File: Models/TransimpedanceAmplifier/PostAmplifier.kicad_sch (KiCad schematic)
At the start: 16 parts, among them Q3 Q_PNP, Q4 Q_NPN, U6 OP37GSZ

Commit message: Save progress
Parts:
- removed JP1: Jumper_2_Bridged, symbol Jumper:Jumper_2_Bridged
- added J1: Conn_01x02_Pin, symbol Connector:Conn_01x02_Pin
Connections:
- net Clamped_Output: now also J1.1 (Pin_1)
- net Feedback_Terminal: now also J1.2 (Pin_2)
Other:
- note added: "Jumper connected by default"
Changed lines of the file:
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@@
 	(text "Cannot \"suppress the influence of transistor\nleakage currents or parasitic capacitances on\nthe input of OP2\" b/c the connection point is\na nonzero voltage instead of GND with this\ndesign. The approach used in the original\npaper would make the diodes conduct from the\nvoltage differential between the connection\npoint and (10k) * (±25 nA) ≈ (±0.25 mV).\n\nInstead, provide a reversible (THT) jumper\nto disconnect this feedback path if it proves\nproblematic. Omit the jumper once we are\ncertain the interference is not a problem."
 		(exclude_from_sim no)
-		(at 71.12 166.37 0)
+		(at 68.072 174.244 0)
 		(effects
 			(font
@@
 			)
 			(justify left)
+		)
+	)
+	(text "Jumper connected by default"
+		(exclude_from_sim no)
+		(at 97.282 142.24 0)
+		(effects
+			(font
+				(size 1.27 1.27)
+			)
 		)
 	)
@@
 	(wire
 		(pts
-			(xy 68.58 137.16) (xy 80.01 137.16)
+			(xy 68.58 139.7) (xy 83.82 139.7)
 		)
 		(stroke
@@
 	(wire
 		(pts
-			(xy 90.17 137.16) (xy 104.14 137.16)
-		)
-		(stroke
-			(width 0)
-			(type default)
-		)
-	)
-	(wire
-		(pts
 			(xy 223.52 78.74) (xy 223.52 91.44)
 		)
@@
 	(wire
 		(pts
+			(xy 86.36 139.7) (xy 124.46 139.7)
+		)
+		(stroke
+			(width 0)
+			(type default)
+		)
+	)
+	(wire
+		(pts
 			(xy 50.8 127) (xy 68.58 127)
 		)
@@
 	(wire
 		(pts
-			(xy 68.58 127) (xy 68.58 137.16)
+			(xy 68.58 127) (xy 68.58 139.7)
 		)
 		(stroke
@@
 	)
 	(label "Clamped_Output"
-		(at 104.14 137.16 0)
+		(at 124.46 139.7 0)
 		(effects
 			(font
@@
 				(path "/ec9f2ae3-e40d-40eb-9760-2b611ee8efd1/226b3d0c-9e45-4bcf-9bef-58938aee743e/1a19fcb8-2301-474b-810f-9788696a69a6"
 					(reference "R9")
-					(unit 1)
-				)
-			)
-		)
-	)
-	(symbol
-		(lib_id "Jumper:Jumper_2_Bridged")
-		(at 85.09 137.16 0)
-		(unit 1)
-		(exclude_from_sim no)
-		(in_bom yes)
-		(on_board yes)
-		(dnp no)
-		(fields_autoplaced yes)
-		(property "Reference" "JP1"
-			(at 85.09 132.08 0)
-			(effects
-				(font
-					(size 1.27 1.27)
-				)
-			)
-		)
-		(property "Value" "Jumper_2_Bridged"
-			(at 85.09 134.62 0)
-			(effects
-				(font
-					(size 1.27 1.27)
-				)
-			)
-		)
-		(property "Footprint" ""
-			(at 85.09 137.16 0)
-			(effects
-				(font
-					(size 1.27 1.27)
-				)
-				(hide yes)
-			)
-		)
-		(property "Datasheet" "~"
-			(at 85.09 137.16 0)
-			(effects
-				(font
-					(size 1.27 1.27)
-				)
-				(hide yes)
-			)
-		)
-		(property "Description" "Jumper, 2-pole, closed/bridged"
-			(at 85.09 137.16 0)
-			(effects
-				(font
-					(size 1.27 1.27)
-				)
-				(hide yes)
-			)
-		)
-		(pin "1"
-		)
-		(pin "2"
-		)
-		(instances
-			(project ""
-				(path "/ec9f2ae3-e40d-40eb-9760-2b611ee8efd1/226b3d0c-9e45-4bcf-9bef-58938aee743e/1a19fcb8-2301-474b-810f-9788696a69a6"
-					(reference "JP1")
 					(unit 1)
 				)
@@
 					(unit 1)
 				)
+			)
+		)
+	)
+	(symbol
+		(lib_id "Connector:Conn_01x02_Pin")
+		(at 86.36 134.62 270)
+		(unit 1)
+		(exclude_from_sim no)
+		(in_bom yes)
+		(on_board yes)
+		(dnp no)
+		(fields_autoplaced yes)
+		(property "Reference" "J1"
+			(at 87.63 133.9849 90)
+			(effects
+				(font
+					(size 1.27 1.27)
+				)
+				(justify left)
+			)
+		)
+		(property "Value" "Conn_01x02_Pin"
+			(at 87.63 136.5249 90)
+			(effects
+				(font
+					(size 1.27 1.27)
+				)
+				(justify left)
+			)
+		)
+		(property "Footprint" ""
+			(at 86.36 134.62 0)
+			(effects
+				(font
+					(size 1.27 1.27)
+				)
+				(hide yes)
+			)
+		)
+		(property "Datasheet" "~"
+			(at 86.36 134.62 0)
+			(effects
+				(font
+					(size 1.27 1.27)
+				)
+				(hide yes)
+			)
+		)
+		(property "Description" "Generic connector, single row, 01x02, script generated"
+			(at 86.36 134.62 0)
+			(effects
+				(font
+					(size 1.27 1.27)
+				)
+				(hide yes)
+			)
+		)
+		(pin "1"
+		)
+		(pin "2"
+		)
+		(instances
+			(project ""
+				(path "/ec9f2ae3-e40d-40eb-9760-2b611ee8efd1/226b3d0c-9e45-4bcf-9bef-58938aee743e/1a19fcb8-2301-474b-810f-9788696a69a6"
+					(reference "J1")
+					(unit 1)
+				)

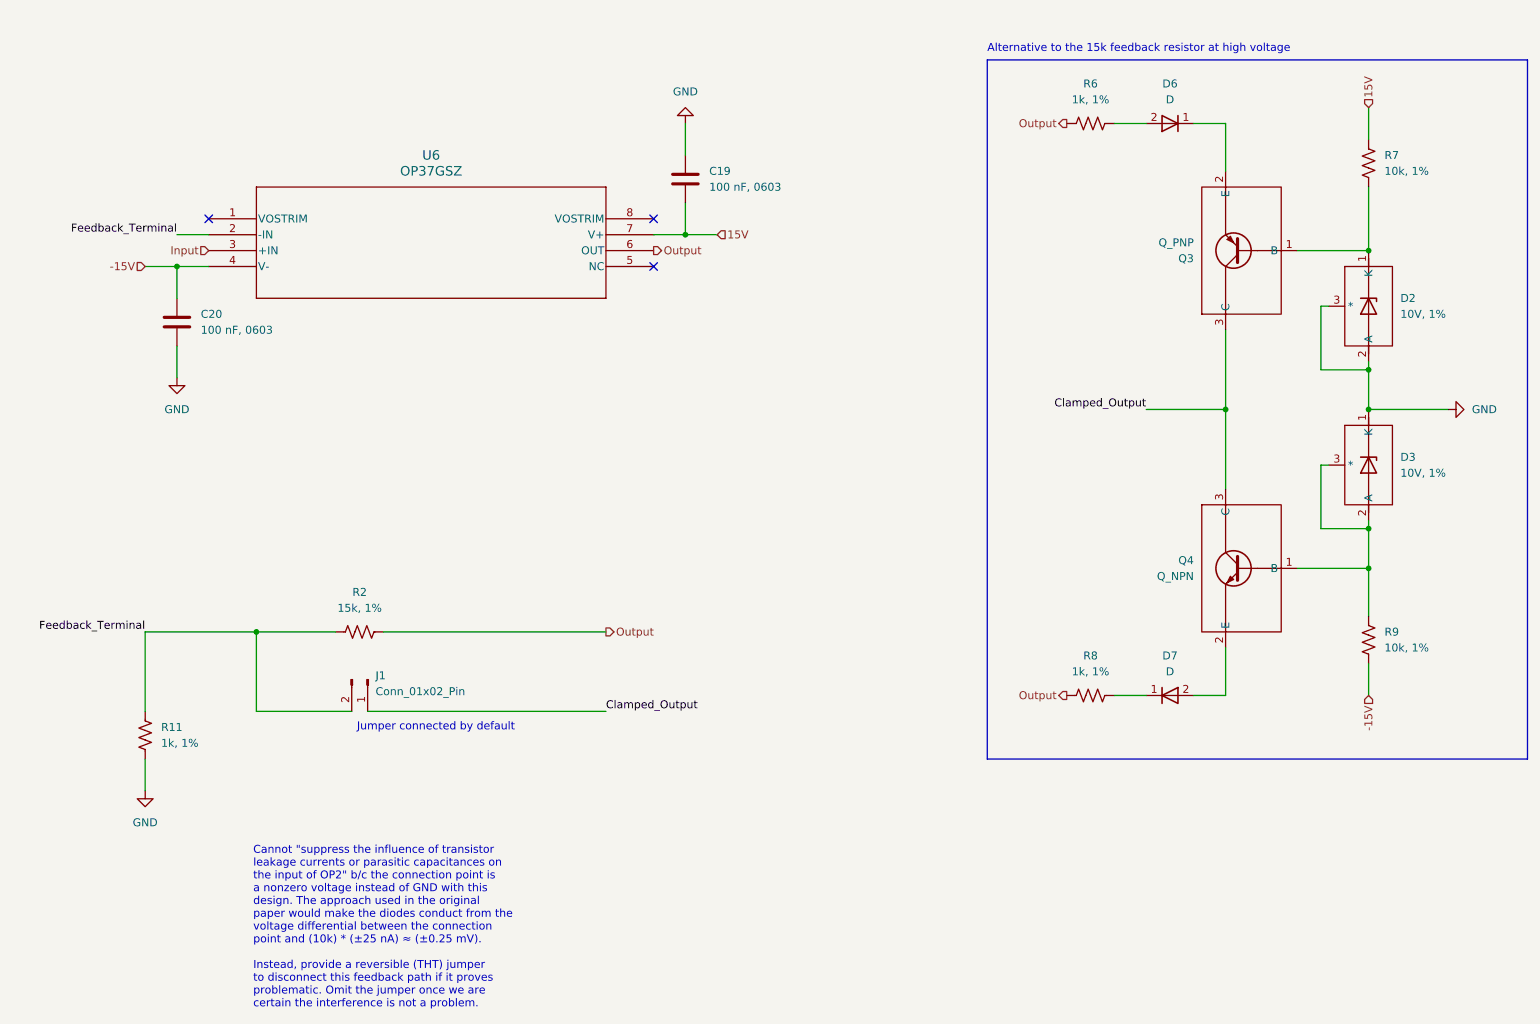
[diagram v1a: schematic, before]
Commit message: This should be all of the pin headers
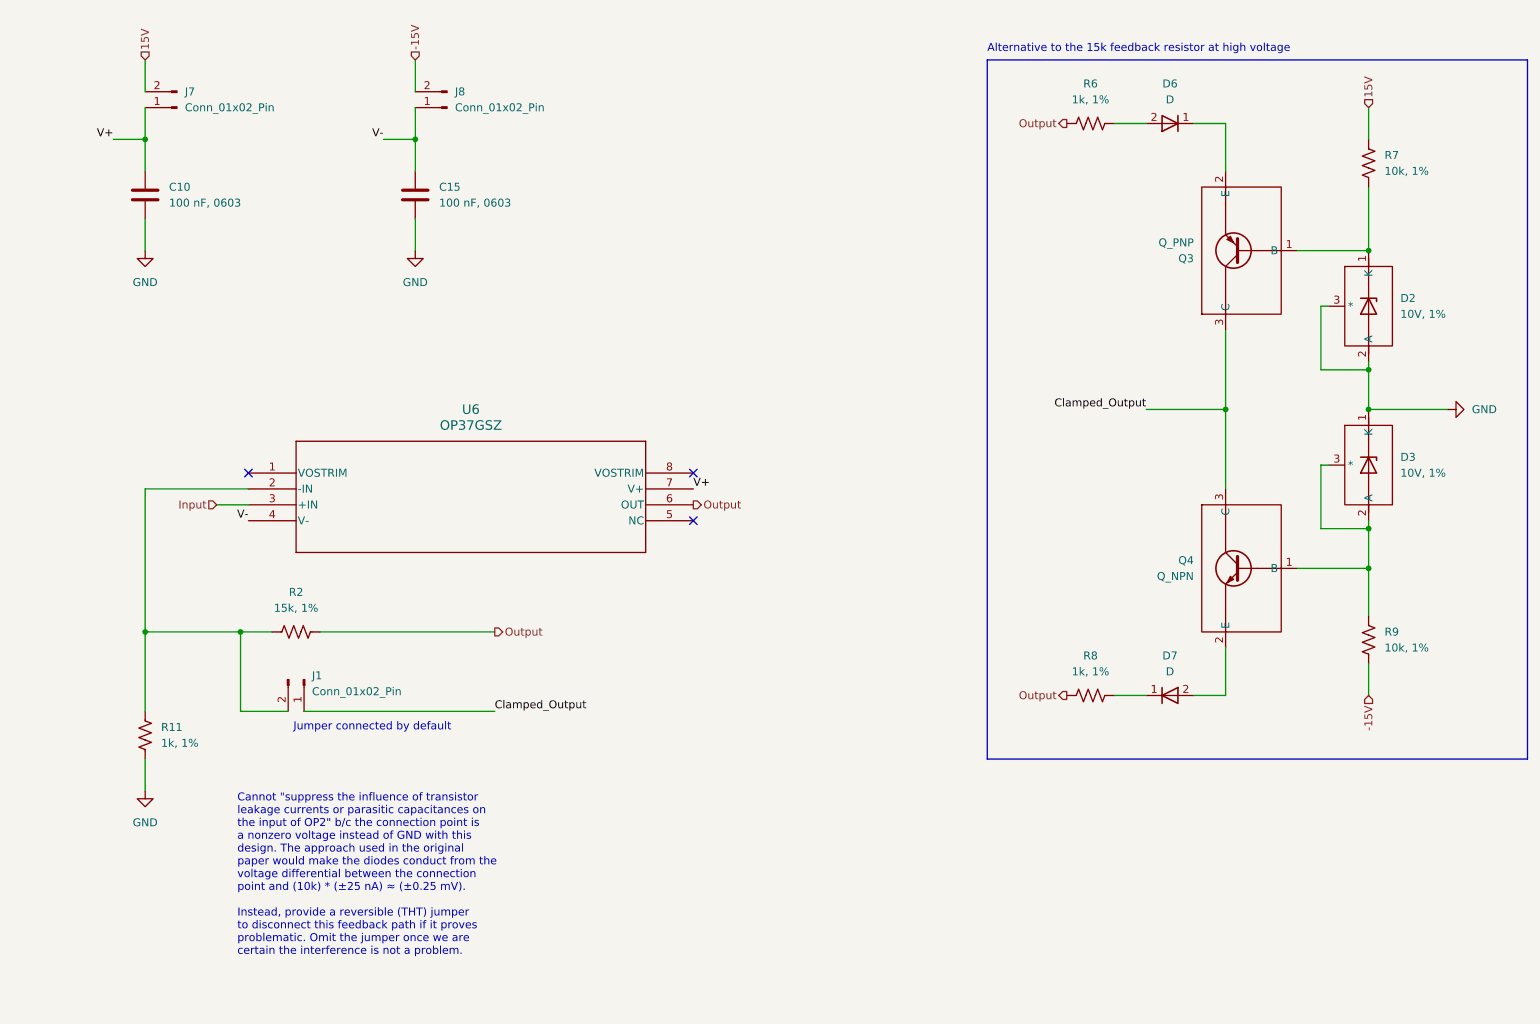
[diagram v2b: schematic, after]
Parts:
- removed C19, C20: 100 nF, 0603, symbol Device:C
- added C10, C15: 100 nF, 0603, symbol Device:C
- added J7, J8: Conn_01x02_Pin, symbol Connector:Conn_01x02_Pin
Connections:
- net -15V: now also J8.2 (Pin_2); no longer U6.4 (V-)
- net 15V: now also J7.2 (Pin_2); no longer U6.7 (V+)
- net GND: now also C10.2, C15.2
- net Feedback_Terminal: no longer names the net of J1.2 (Pin_2), R11.2, R2.1, U6.2 (-IN)
- new net V+: C10.1, J7.1 (Pin_1), U6.7 (V+)
- new net V-: C15.1, J8.1 (Pin_1), U6.4 (V-)
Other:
- moved on the sheet: J1, R2, U6

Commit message: Save progress
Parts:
- J1, J7, J8: Purchase Link (none) -> https://www.digikey.com/en/products/detail/sullins-connecto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
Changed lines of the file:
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@@
+			)
+		)
+		(property "Purchase Link" "https://www.digikey.com/en/products/detail/sullins-connector-solutions/QPC02SXGN-RC/2618262"
+			(at 55.88 43.18 0)
+			(effects
+				(font
+					(size 1.27 1.27)
+				)
+				(hide yes)
 			)
 		)
@@
 			)
 		)
+		(property "Purchase Link" "https://www.digikey.com/en/products/detail/sullins-connector-solutions/QPC02SXGN-RC/2618262"
+			(at 76.2 134.62 90)
+			(effects
+				(font
+					(size 1.27 1.27)
+				)
+				(hide yes)
+			)
+		)
 		(pin "1"
 		)
@@
 			(at 99.06 43.18 0)
 			(effects
+				(font
+					(size 1.27 1.27)
+				)
+				(hide yes)
+			)
+		)
+		(property "Purchase Link" "https://www.digikey.com/en/products/detail/sullins-connector-solutions/QPC02SXGN-RC/2618262"
+			(at 99.06 43.18 0)
+			(effects

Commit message: Save progress
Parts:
- U6: footprint R_8_ADI -> (none)
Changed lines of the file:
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@@
 			)
 		)
-		(property "Footprint" "R_8_ADI"
+		(property "Footprint" ""
 			(at 67.31 101.6 0)
 			(effects

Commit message: Save progress
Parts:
- U6: value OP37GSZ -> OP37G
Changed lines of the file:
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@@
 			)
 		)
-		(property "Value" "OP37GSZ"
+		(property "Value" "OP37G"
 			(at 102.87 93.98 0)
 			(effects
